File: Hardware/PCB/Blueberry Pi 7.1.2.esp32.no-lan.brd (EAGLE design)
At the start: 80.7 x 60.9 mm, 208 parts, among them J2 AUDIO_JACK_SMD, J3 USB-A-FEMALE, Q1 24Mhz, Q2 32kHz, Q3 IRLML2402, Q4 IRLML2402, U1 SN65LVDS84AQDGGRQ1, U2 W25Q32FV, U3 AP3031KTR-G1, U4 ESP-WROOM-32, X1 FH12-50S-0.5SH, X2 87758-1216

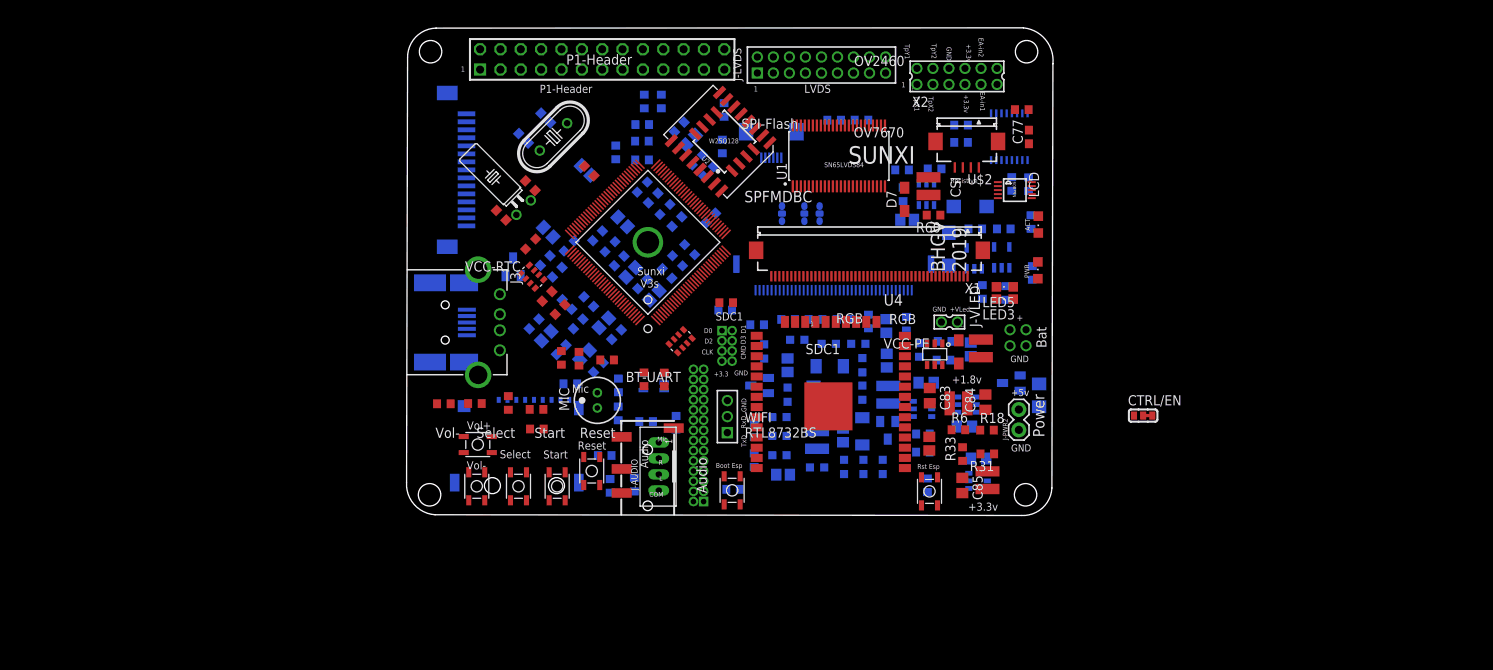
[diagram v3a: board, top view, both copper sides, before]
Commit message: (not finished yet) checks and new choise with SIM800C gsm module
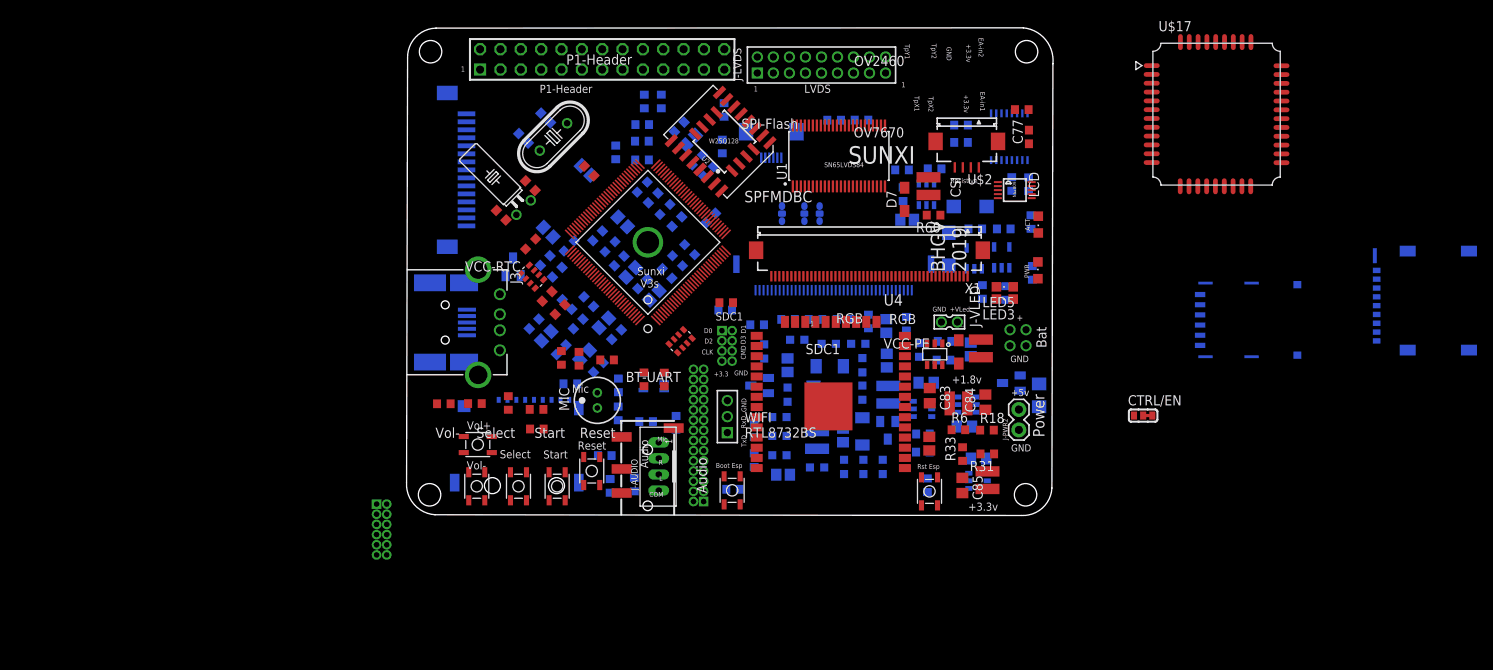
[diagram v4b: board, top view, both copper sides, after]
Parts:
- removed X2: 87758-1216, con-molex:87758-1216
- added J1: (no value), Wurth_Elektronik_Electromechanic_Input-Output_Connectors_rev16b:693023010811
- added J5: (no value), Wurth_Elektronik_Electromechanic_Input-Output_Connectors_rev16b:693043020611
- added U$17: SIM800C, SIM800C:SIM800C
- added U$18: HDR-1.27MM-62, headers-1.27:HDR-1.27MM-6*2
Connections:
- removed net N$4: D2.C, D6.C, L4.P$1, R59.2
- new net SIM_VDD: U$17.18
- new net VBAT: U$17.34, U$17.35
- new net VBUS: U$17.24
- new net VEXT: U$17.40
- new net VRTC: U$17.28
- net +3V3: now also U$16.3, U$18.P$7, U$18.P$8; no longer X2.7, X2.8
- net EA-IN1: now also U$18.P$9; no longer X2.9
- net EA-IN2: now also U$18.P$10; no longer X2.10
- net GND: now also U$17.13, U$17.19, U$17.21, U$17.27, U$17.30, U$17.31, U$17.33, U$17.36, U$17.37, U$17.8, U$18.P$5, U$18.P$6; no longer X2.5, X2.6
- net N$14: now also D2.C, D6.C, L4.P$1, R59.2
- net TPX1: now also U$18.P$1; no longer X2.1
- net TPX2: now also U$18.P$3; no longer X2.3
- net TPY1: now also U$18.P$2; no longer X2.2
- net TPY2: now also U$18.P$4; no longer X2.4
- net VIB1: now also U$18.P$11; no longer X2.11
- net VIB2: now also U$18.P$12; no longer X2.12
